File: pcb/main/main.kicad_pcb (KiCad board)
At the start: 2 copper layers, 70 x 65 mm, 102 parts, among them J1 UART, J101 USB_C_Receptacle_USB2.0_16P, J2 JTAG, J3 JTAG SRC, J4 26 pin IDC, J5 Conn_01x06, J6 I2C, Q101 Q_Dual_PMOS_S1G1S2G2D2D2D1D1, Q122 DMP3099L, Q131 FDC6312P, SW1 Boot, SW2 Reset, U1 74LVC1G17, U101 USBLC6-2SC6, U102 TS3USB221A, U103 CYPD3176, U121 TPS63070, U131 TPS629203, U2 74LVC1G17, U3 ESP32-S3-WROOM-1

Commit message: Parts updates, a few board tweaks
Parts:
- R104: value 49.9K -> 100k
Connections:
- net /3v3/FB_{3.3V} renamed /3v3/FB_{3V3}
- net /3v3/L1_{3.3V} renamed /3v3/SW_{3V3A}
- net /3v3/L2_{3.3V} renamed /3v3/SW_{3V3B}
- net /3v3/VAUX_{3.3V} renamed /3v3/V_{AUX}
- net /3v3/VIN_{3.3V} renamed /3v3/V_{IN3.3V}
- net /5v/MODE_{5V} renamed /5v/FB_{MODE}
- net /5v/VSET_{5V} renamed /5v/FB_{5V}
- net /usb/GATE renamed /usb/G_{USB}
- net /usb/SOURCE renamed /usb/S_{USB}
- net /usb/VBUS_{C} renamed /usb/V_{BUSC}
- net Net-(U103-ISNK_FINE) renamed /usb/FB_{ISINKF}
- net Net-(U103-VBUS_MAX) renamed /usb/FB_{VBUSMAX}
- net Net-(U103-VCCD) renamed /usb/V_{CCD}
- net VCC_{UART} renamed V_{UART}
- net VDDD renamed V_{DDD}

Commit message: Update fab attributes, update silscreen to include step
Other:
- board text added: "${TITLE}//REV ${REV}${STEP}//${AUTHOR}"
- board text removed: "${TITLE}//REV ${REV}//${AUTHOR}"
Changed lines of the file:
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@@
 		(capping no)
 		(filling no)
-		(zone_defaults)
 		(pcbplotparams
 			(layerselection 0x00000000_00000000_55555555_5755f5ff)
@@
 	(property "AUTHOR" "Jason Watkins")
 	(property "REV" "C")
+	(property "STEP" "1")
 	(property "TITLE" "4 Digit Nixie Clock Controller")
 	(footprint "TestPoint:TestPoint_Pad_D1.0mm"
@@
 		)
 	)
-	(gr_text "${TITLE}//REV ${REV}//${AUTHOR}\n"
+	(gr_text "${TITLE}//REV ${REV}${STEP}//${AUTHOR}\n"
 		(at 168 58 0)
 		(layer "B.SilkS")

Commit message: Update ins1 tube model, update hv/main connector to 1 vbus, 2 gnd connections, update hv inhibit circuit to be default inhibit and require positive enable from MCU
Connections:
- net ~{EN}_{HV} renamed EN_{HV}
- J4 pad 10: unconnected-(J4-Pin_10-Pad10) -> GND
- J4 pad 17: unconnected-(J4-Pin_17-Pad17) -> GND
- J4 pad 18: unconnected-(J4-Pin_18-Pad18) -> GND
- J4 pad 9: unconnected-(J4-Pin_9-Pad9) -> GND
- J5 pad 4: V_{BUS} -> GND
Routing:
- net V_{BUS}: track 99.1 -> 95.8 mm

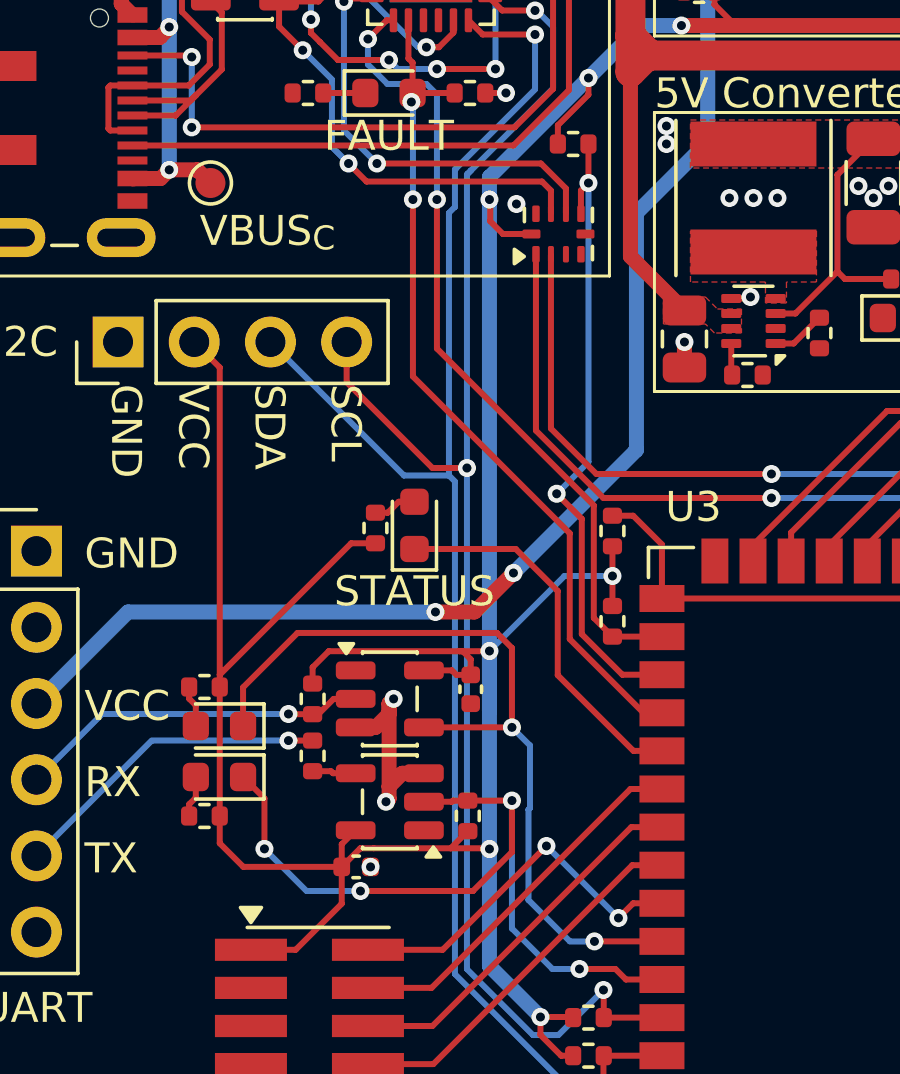
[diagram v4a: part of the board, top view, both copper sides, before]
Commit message: Bump main to Rev D1, add EN_USB jumper to board, fix UART LED locations.
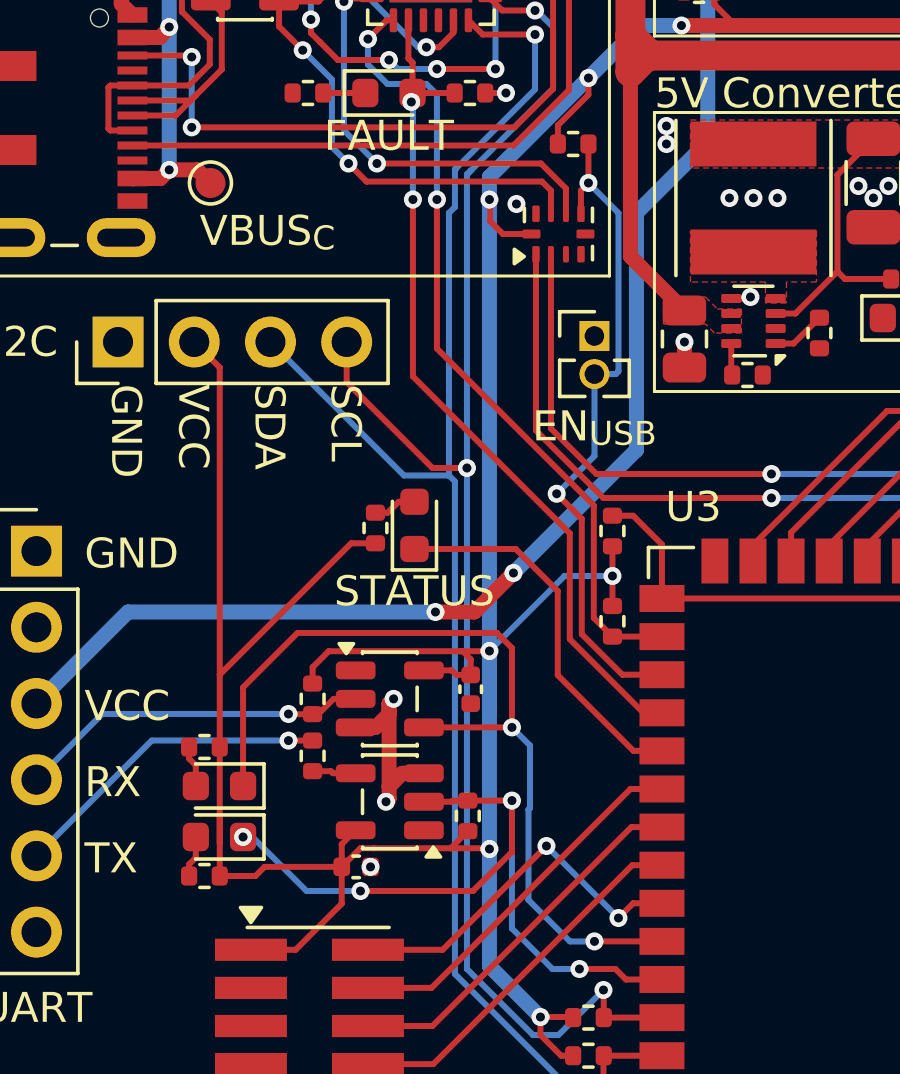
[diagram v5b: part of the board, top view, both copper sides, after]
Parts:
- added J7: EN_{USB}, Connector_PinHeader_1.27mm:PinHeader_1x02_P1.27mm_Vertical, F.Cu at (122.0, 87.0)
- Q101: value Q_Dual_PMOS_S1G1S2G2D2D2D1D1 -> FDS4935A
- moved D1 2.00 mm to (109.5, 103.7)
- moved D2 2.00 mm to (109.5, 102.0)
- moved R3 2.00 mm to (109.0, 105.0)
- moved R4 2.00 mm to (109.0, 100.7)
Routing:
- net /mcu/RXD0: track 27.8 -> 29.8 mm
- net /mcu/TXD0: track 26.7 -> 24.9 mm
- net +3V3: track 211.4 -> 213.2 mm
- net ~{EN}_{USB}: track 21.5 -> 22.7 mm

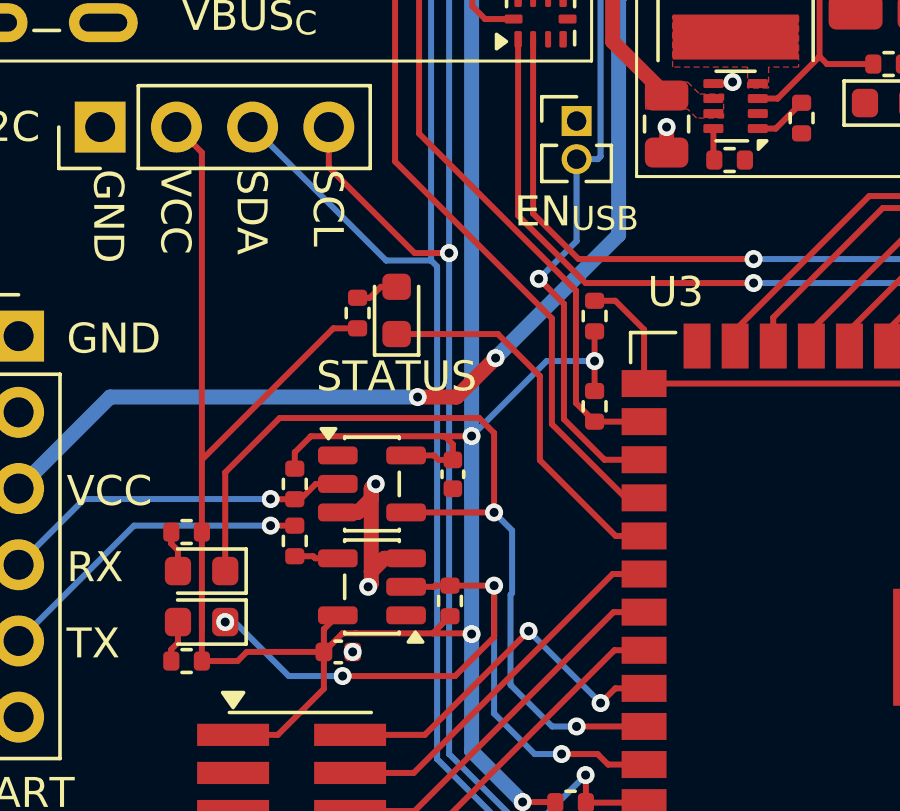
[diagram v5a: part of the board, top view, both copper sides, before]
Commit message: Tweaks to the new jumper
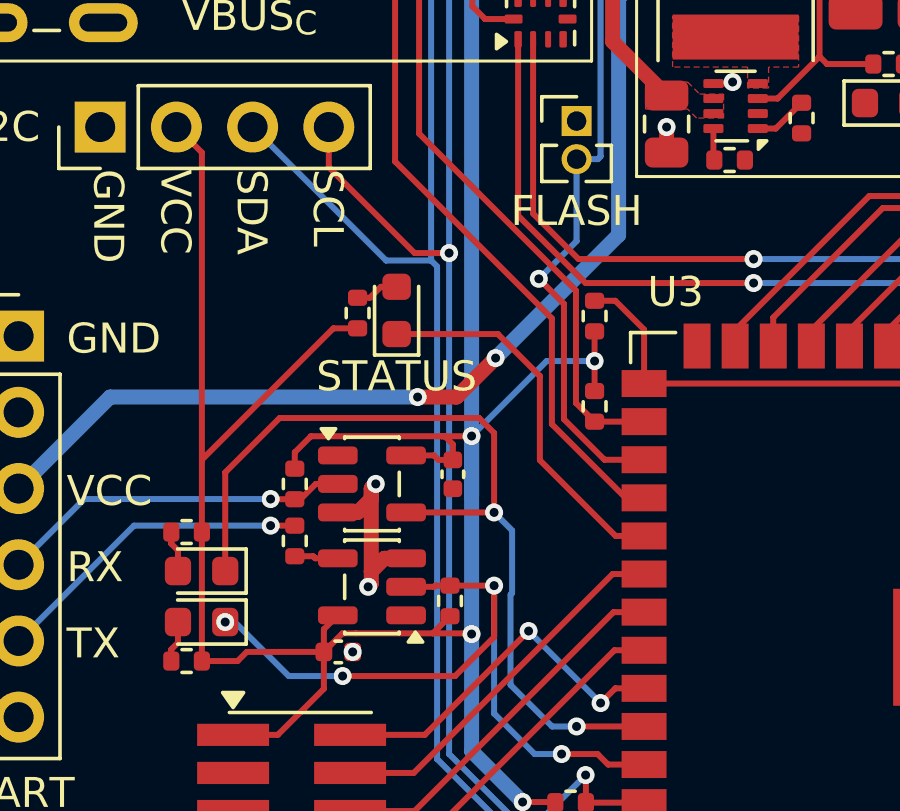
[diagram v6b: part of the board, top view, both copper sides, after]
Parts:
- J7: value EN_{USB} -> FLASH
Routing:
- net +3V3: track 213.2 -> 212.3 mm
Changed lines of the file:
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@@
 			)
 		)
-		(property "Value" "EN_{USB}"
-			(at 0 3.015 0)
+		(property "Value" "FLASH"
+			(at 0 3 0)
 			(layer "F.SilkS")
 			(effects
@@
 	)
 	(segment
-		(start 109.51 105)
-		(end 109.51 100.7)
-		(width 0.2)
-		(layer "F.Cu")
-		(net "+3V3")
-	)
-	(segment
 		(start 118.5 82.451)
 		(end 118.525 82.476)
@@
 	)
 	(segment
-		(start 114.196 104.076)
-		(end 114.6425 104.076)
+		(start 109.51 105)
+		(end 109.51 100.7)
 		(width 0.2)
 		(layer "F.Cu")
@@
 	)
 	(segment
-		(start 126 75.5)
-		(end 126 75.951)
+		(start 114.196 104.076)
+		(end 114.6425 104.076)
 		(width 0.2)
 		(layer "F.Cu")
@@
 	)
 	(segment
-		(start 109.51 103.91)
-		(end 109.51 103)
+		(start 126 75.5)
+		(end 126 75.951)
 		(width 0.2)
 		(layer "F.Cu")
